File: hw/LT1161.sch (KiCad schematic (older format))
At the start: 6 parts, among them U501 MOSFET_DRIVER_LT1161, U502 MOSFET_IPG20N04S4L11ATMA1, U503 MOSFET_IPG20N04S4L11ATMA1

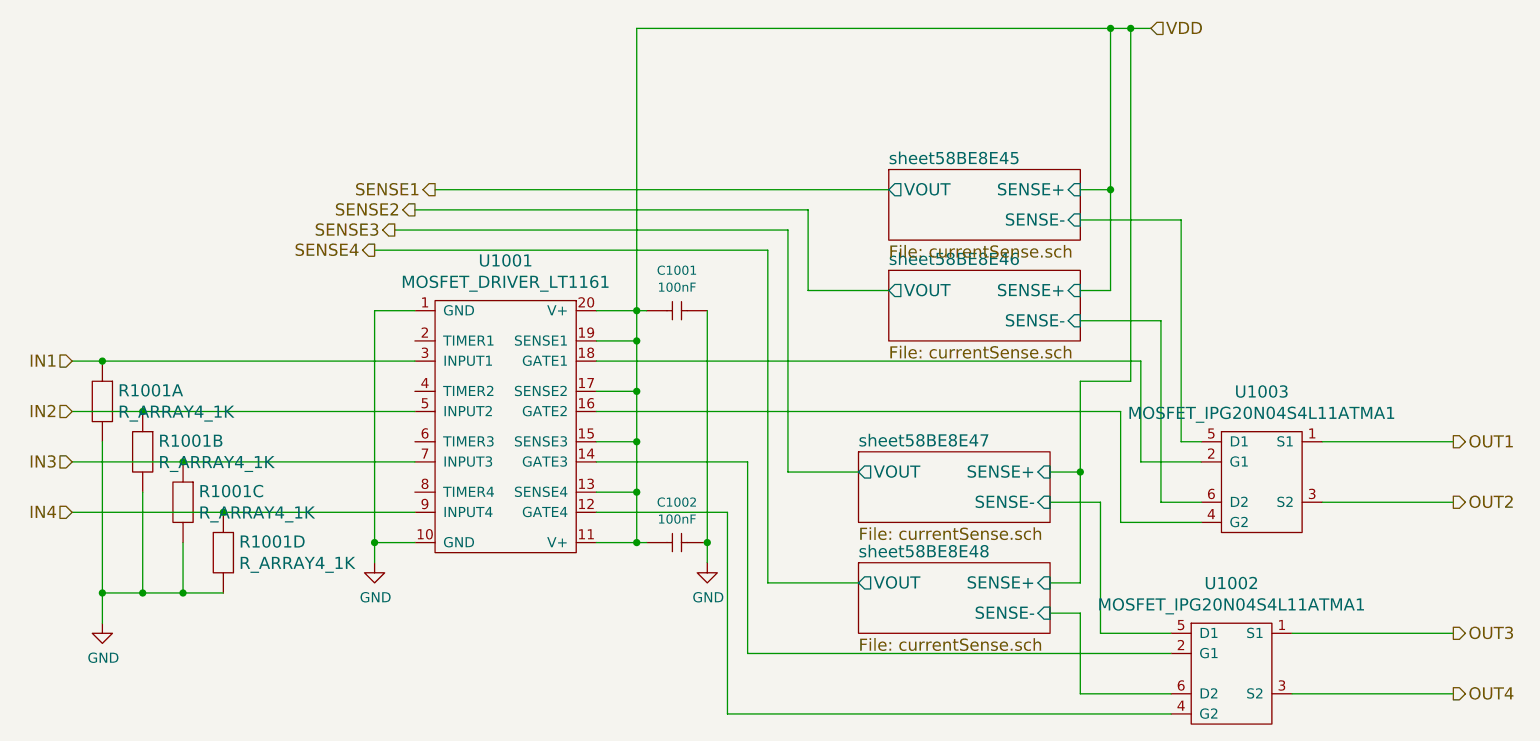
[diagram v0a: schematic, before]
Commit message: first pcb revision ready to order
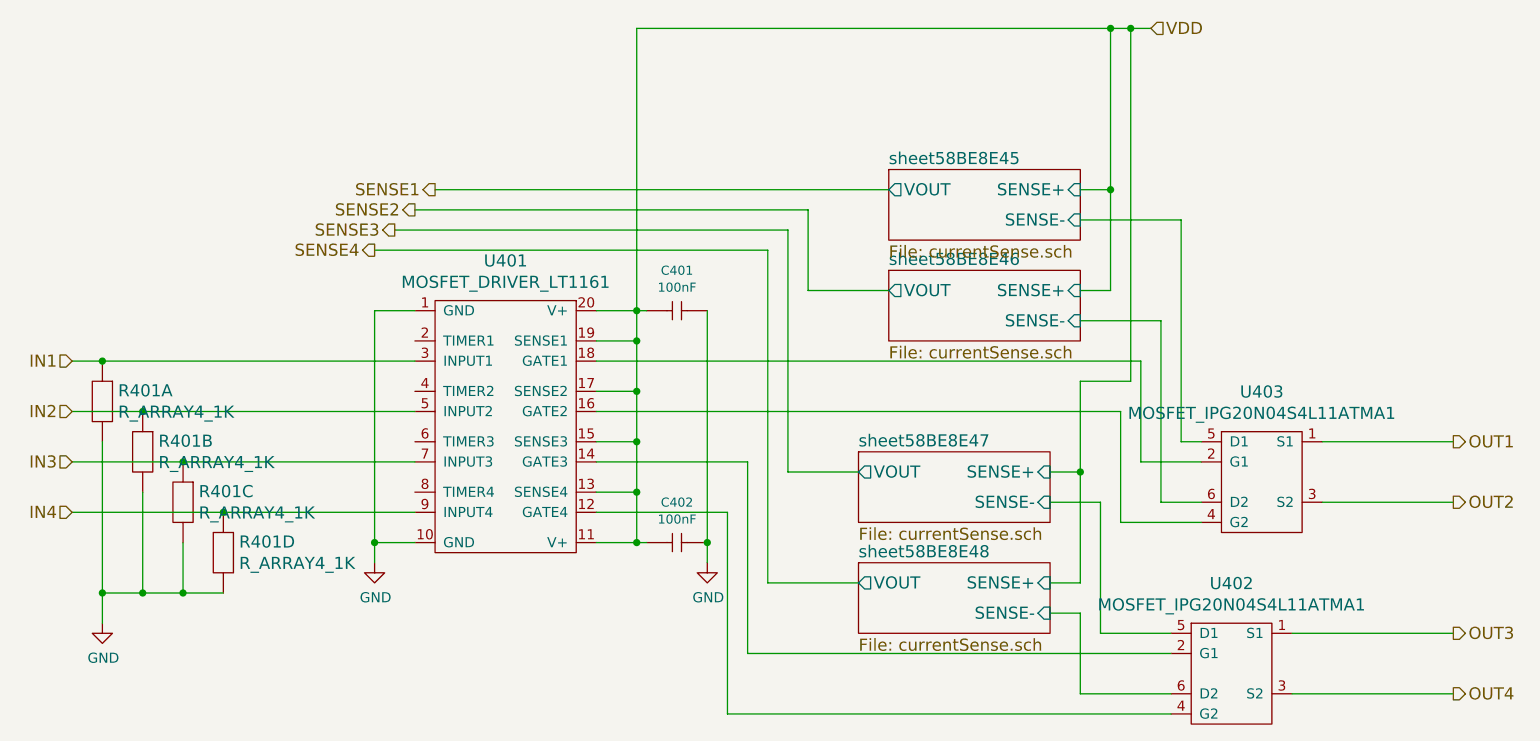
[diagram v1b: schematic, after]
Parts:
- removed U501: MOSFET_DRIVER_LT1161, usevolt:SO20, symbol MOSFET_DRIVER_LT1161
- removed U502: MOSFET_IPG20N04S4L11ATMA1, usevolt:PG-TDSON-8-4, symbol MOSFET_IPG20N04S4L11ATMA1
- added U401: MOSFET_DRIVER_LT1161, usevolt:SO20, symbol MOSFET_DRIVER_LT1161
- added U402: MOSFET_IPG20N04S4L11ATMA1, usevolt:PG-TDSON-8-4, symbol MOSFET_IPG20N04S4L11ATMA1
- renumbered C501 to C401, C502 to C402, R501 to R401, U503 to U403
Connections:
- net GND: now also U401.1 (GND), U401.10 (GND)
- net IN1: now also U401.3 (INPUT1)
- net IN2: now also U401.5 (INPUT2)
- net IN3: now also U401.7 (INPUT3)
- net IN4: now also U401.9 (INPUT4)
- net OUT3: now also U402.1 (S1)
- net OUT4: now also U402.3 (S2)
- net VDD: now also U401.11 (V+), U401.13 (SENSE4), U401.15 (SENSE3), U401.17 (SENSE2), U401.19 (SENSE1), U401.20 (V+)
- net sheet58BE8E47/SENSE-: now also U402.5 (D1)
- net sheet58BE8E48/SENSE-: now also U402.6 (D2)
- net at U403.4 (G2): now also U401.16 (GATE2)
- net at U403.2 (G1): now also U401.18 (GATE1)
- new net: U401.12 (GATE4), U402.4 (G2)
- new net: U401.14 (GATE3), U402.2 (G1)
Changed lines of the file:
@@
 LIBS:usevolt
 LIBS:wurth_elektronik_LED
+LIBS:csb-cache
 EELAYER 26 0
 EELAYER END
@@
 $Sheet
 S 6300 2700 950  350
-U 58BE8E4D
+U 595CED4D
 F0 "sheet58BE8E45" 60
 F1 "currentSense.sch" 60
@@
 $EndSheet
 $Comp
-L GND #PWR502
-U 1 1 58BE8E62
+L GND #PWR021
+U 1 1 595CED4E
 P 3750 4650
-AR Path="/58BE52C9/58BE8E62" Ref="#PWR502"  Part="1"
-AR Path="/58C7B0A8/58BE8E62" Ref="#PWR1002"  Part="1"
-AR Path="/59542AAB/58BE8E62" Ref="#PWR1002"  Part="1"
-AR Path="/5954FB0E/58BE8E62" Ref="#PWR1002"  Part="1"
-F 0 "#PWR1002" H 3750 4400 50  0001 C CNN
+F 0 "#PWR021" H 3750 4400 50  0001 C CNN
 F 1 "GND" H 3755 4477 50  0000 C CNN
 F 2 "" H 3750 4650 50  0000 C CNN
@@
 $EndComp
 $Comp
-L MOSFET_DRIVER_LT1161 U501
-U 1 1 58BE8E74
+L MOSFET_DRIVER_LT1161 U401
+U 1 1 595CED4F
 P 4400 3950
-AR Path="/58BE52C9/58BE8E74" Ref="U501"  Part="1"
-AR Path="/58C7B0A8/58BE8E74" Ref="U1001"  Part="1"
-AR Path="/59542AAB/58BE8E74" Ref="U1001"  Part="1"
-AR Path="/5954FB0E/58BE8E74" Ref="U1001"  Part="1"
-F 0 "U1001" H 4400 4747 60  0000 C CNN
+F 0 "U401" H 4400 4747 60  0000 C CNN
 F 1 "MOSFET_DRIVER_LT1161" H 4400 4641 60  0000 C CNN
 F 2 "usevolt:SO20" H 4450 4825 60  0001 C CNN
@@
 P 5200 3400
 AR Path="/58BE8EAF" Ref="C?"  Part="1"
-AR Path="/58BE52C9/58BE8EAF" Ref="C501"  Part="1"
-AR Path="/58C7B0A8/58BE8EAF" Ref="C1001"  Part="1"
-AR Path="/59542AAB/58BE8EAF" Ref="C1001"  Part="1"
-AR Path="/5954FB0E/58BE8EAF" Ref="C1001"  Part="1"
-F 0 "C1001" H 5250 3599 45  0000 C CNN
+AR Path="/58BE52C9/58BE8EAF" Ref="C?"  Part="1"
+AR Path="/58C7B0A8/58BE8EAF" Ref="C?"  Part="1"
+AR Path="/59542AAB/58BE8EAF" Ref="C401"  Part="1"
+AR Path="/5954FB0E/58BE8EAF" Ref="C?"  Part="1"
+F 0 "C401" H 5250 3599 45  0000 C CNN
 F 1 "100nF" H 5250 3515 45  0000 C CNN
 F 2 "kemet:0603" H 5230 3550 20  0001 C CNN
@@
 P 5200 4550
 AR Path="/58BE8EBA" Ref="C?"  Part="1"
-AR Path="/58BE52C9/58BE8EBA" Ref="C502"  Part="1"
-AR Path="/58C7B0A8/58BE8EBA" Ref="C1002"  Part="1"
-AR Path="/59542AAB/58BE8EBA" Ref="C1002"  Part="1"
-AR Path="/5954FB0E/58BE8EBA" Ref="C1002"  Part="1"
-F 0 "C1002" H 5250 4749 45  0000 C CNN
+AR Path="/58BE52C9/58BE8EBA" Ref="C?"  Part="1"
+AR Path="/58C7B0A8/58BE8EBA" Ref="C?"  Part="1"
+AR Path="/59542AAB/58BE8EBA" Ref="C402"  Part="1"
+AR Path="/5954FB0E/58BE8EBA" Ref="C?"  Part="1"
+F 0 "C402" H 5250 4749 45  0000 C CNN
 F 1 "100nF" H 5250 4665 45  0000 C CNN
 F 2 "kemet:0603" H 5230 4700 20  0001 C CNN
@@
 $EndComp
 $Comp
-L GND #PWR503
-U 1 1 58BE8EC1
+L GND #PWR022
+U 1 1 595CED54
 P 5400 4650
-AR Path="/58BE52C9/58BE8EC1" Ref="#PWR503"  Part="1"
-AR Path="/58C7B0A8/58BE8EC1" Ref="#PWR1003"  Part="1"
-AR Path="/59542AAB/58BE8EC1" Ref="#PWR1003"  Part="1"
-AR Path="/5954FB0E/58BE8EC1" Ref="#PWR1003"  Part="1"
-F 0 "#PWR1003" H 5400 4400 50  0001 C CNN
+F 0 "#PWR022" H 5400 4400 50  0001 C CNN
 F 1 "GND" H 5405 4477 50  0000 C CNN
 F 2 "" H 5400 4650 50  0000 C CNN
@@
 Connection ~ 7250 4200
 $Comp
-L MOSFET_IPG20N04S4L11ATMA1 U502
-U 1 1 591C1D78
+L MOSFET_IPG20N04S4L11ATMA1 U402
+U 1 1 595CED55
 P 8000 5200
-AR Path="/58BE52C9/591C1D78" Ref="U502"  Part="1"
-AR Path="/58C7B0A8/591C1D78" Ref="U1002"  Part="1"
-AR Path="/59542AAB/591C1D78" Ref="U1002"  Part="1"
-AR Path="/5954FB0E/591C1D78" Ref="U1002"  Part="1"
-F 0 "U1002" H 8000 5647 60  0000 C CNN
+F 0 "U402" H 8000 5647 60  0000 C CNN
 F 1 "MOSFET_IPG20N04S4L11ATMA1" H 8000 5541 60  0000 C CNN
 F 2 "usevolt:PG-TDSON-8-4" H 8000 5700 60  0001 C CNN
@@
 $EndComp
 $Comp
-L MOSFET_IPG20N04S4L11ATMA1 U503
+L MOSFET_IPG20N04S4L11ATMA1 U403
 U 1 1 591C1E34
 P 8150 4250
-AR Path="/58BE52C9/591C1E34" Ref="U503"  Part="1"
-AR Path="/58C7B0A8/591C1E34" Ref="U1003"  Part="1"
-AR Path="/59542AAB/591C1E34" Ref="U1003"  Part="1"
-AR Path="/5954FB0E/591C1E34" Ref="U1003"  Part="1"
-F 0 "U1003" H 8150 4697 60  0000 C CNN
+F 0 "U403" H 8150 4697 60  0000 C CNN
 F 1 "MOSFET_IPG20N04S4L11ATMA1" H 8150 4591 60  0000 C CNN
 F 2 "usevolt:PG-TDSON-8-4" H 8150 4750 60  0001 C CNN
@@
 $EndComp
 $Comp
-L R_ARRAY4_1K R501
+L R_ARRAY4_1K R401
 U 1 1 593FBF1A
 P 2400 3850
-AR Path="/58BE52C9/593FBF1A" Ref="R501"  Part="1"
-AR Path="/58C7B0A8/593FBF1A" Ref="R1001"  Part="1"
-AR Path="/59542AAB/593FBF1A" Ref="R1001"  Part="1"
-AR Path="/5954FB0E/593FBF1A" Ref="R1001"  Part="1"
-F 0 "R1001" V 2347 3928 60  0000 L CNN
+F 0 "R401" V 2347 3928 60  0000 L CNN
 F 1 "R_ARRAY4_1K" V 2453 3928 60  0000 L CNN
 F 2 "usevolt:0603_array4" H 2300 3950 60  0001 C CNN
@@
 $EndComp
 $Comp
-L R_ARRAY4_1K R501
+L R_ARRAY4_1K R401
 U 2 1 593FBFF5
 P 2600 4100
-AR Path="/58BE52C9/593FBFF5" Ref="R501"  Part="2"
-AR Path="/58C7B0A8/593FBFF5" Ref="R1001"  Part="2"
-AR Path="/59542AAB/593FBFF5" Ref="R1001"  Part="2"
-AR Path="/5954FB0E/593FBFF5" Ref="R1001"  Part="2"
-F 0 "R1001" V 2547 4178 60  0000 L CNN
+F 0 "R401" V 2547 4178 60  0000 L CNN
 F 1 "R_ARRAY4_1K" V 2653 4178 60  0000 L CNN
 F 2 "usevolt:0603_array4" H 2500 4200 60  0001 C CNN
@@
 $EndComp
 $Comp
-L R_ARRAY4_1K R501
+L R_ARRAY4_1K R401
 U 3 1 593FC0D3
 P 2800 4350
-AR Path="/58BE52C9/593FC0D3" Ref="R501"  Part="3"
-AR Path="/58C7B0A8/593FC0D3" Ref="R1001"  Part="3"
-AR Path="/59542AAB/593FC0D3" Ref="R1001"  Part="3"
-AR Path="/5954FB0E/593FC0D3" Ref="R1001"  Part="3"
-F 0 "R1001" V 2747 4428 60  0000 L CNN
+F 0 "R401" V 2747 4428 60  0000 L CNN
 F 1 "R_ARRAY4_1K" V 2853 4428 60  0000 L CNN
 F 2 "usevolt:0603_array4" H 2700 4450 60  0001 C CNN
@@
 $EndComp
 $Comp
-L R_ARRAY4_1K R501
+L R_ARRAY4_1K R401
 U 4 1 593FC1B8
 P 3000 4600
-AR Path="/58BE52C9/593FC1B8" Ref="R501"  Part="4"
-AR Path="/58C7B0A8/593FC1B8" Ref="R1001"  Part="4"
-AR Path="/59542AAB/593FC1B8" Ref="R1001"  Part="4"
-AR Path="/5954FB0E/593FC1B8" Ref="R1001"  Part="4"
-F 0 "R1001" V 2947 4678 60  0000 L CNN
+F 0 "R401" V 2947 4678 60  0000 L CNN
 F 1 "R_ARRAY4_1K" V 3053 4678 60  0000 L CNN
 F 2 "usevolt:0603_array4" H 2900 4700 60  0001 C CNN
@@
 Connection ~ 2400 3650
 $Comp
-L GND #PWR501
+L GND #PWR023
 U 1 1 593FC6CE
 P 2400 4950
-AR Path="/58BE52C9/593FC6CE" Ref="#PWR501"  Part="1"
-AR Path="/58C7B0A8/593FC6CE" Ref="#PWR1001"  Part="1"
-AR Path="/59542AAB/593FC6CE" Ref="#PWR1001"  Part="1"
-AR Path="/5954FB0E/593FC6CE" Ref="#PWR1001"  Part="1"
-F 0 "#PWR1001" H 2400 4700 50  0001 C CNN
+F 0 "#PWR023" H 2400 4700 50  0001 C CNN
 F 1 "GND" H 2405 4777 50  0000 C CNN
 F 2 "" H 2400 4950 50  0000 C CNN
